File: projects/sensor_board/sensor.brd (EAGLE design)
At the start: 90.2 x 95.9 mm, 49 parts, among them J1 504050-0791, J2 FH28-10S-0.5SH_05_, J3 504050-0791, J4 504050-1091, J5 504050-0791, J6 504050-0791, U1 NXP_FXAS21002CQR1NXP_FXAS2100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, U2 HONEYWELL_HMC5983-TRHONEYWELL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, U3 DS1307N, U4 NXP_FXAS21002CQR1NXP_FXAS2100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, U5 HONEYWELL_HMC5983-TRHONEYWELL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, U6 NXP_FXAS21002CQR1NXP_FXAS2100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, U7 HONEYWELL_HMC5983-TRHONEYWELL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, Y1 ECS-.327-12.5-13X

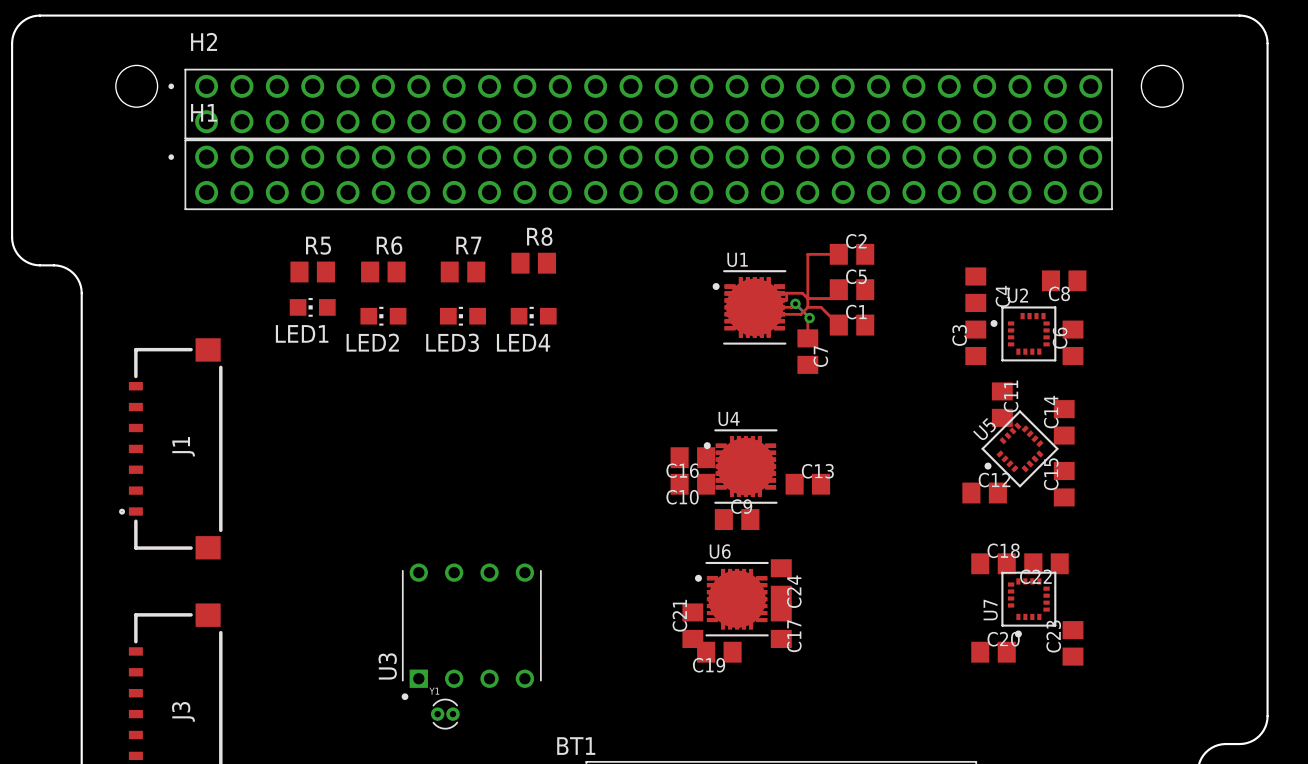
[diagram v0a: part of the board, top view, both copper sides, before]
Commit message: Updates to sensor board. Routed sensors
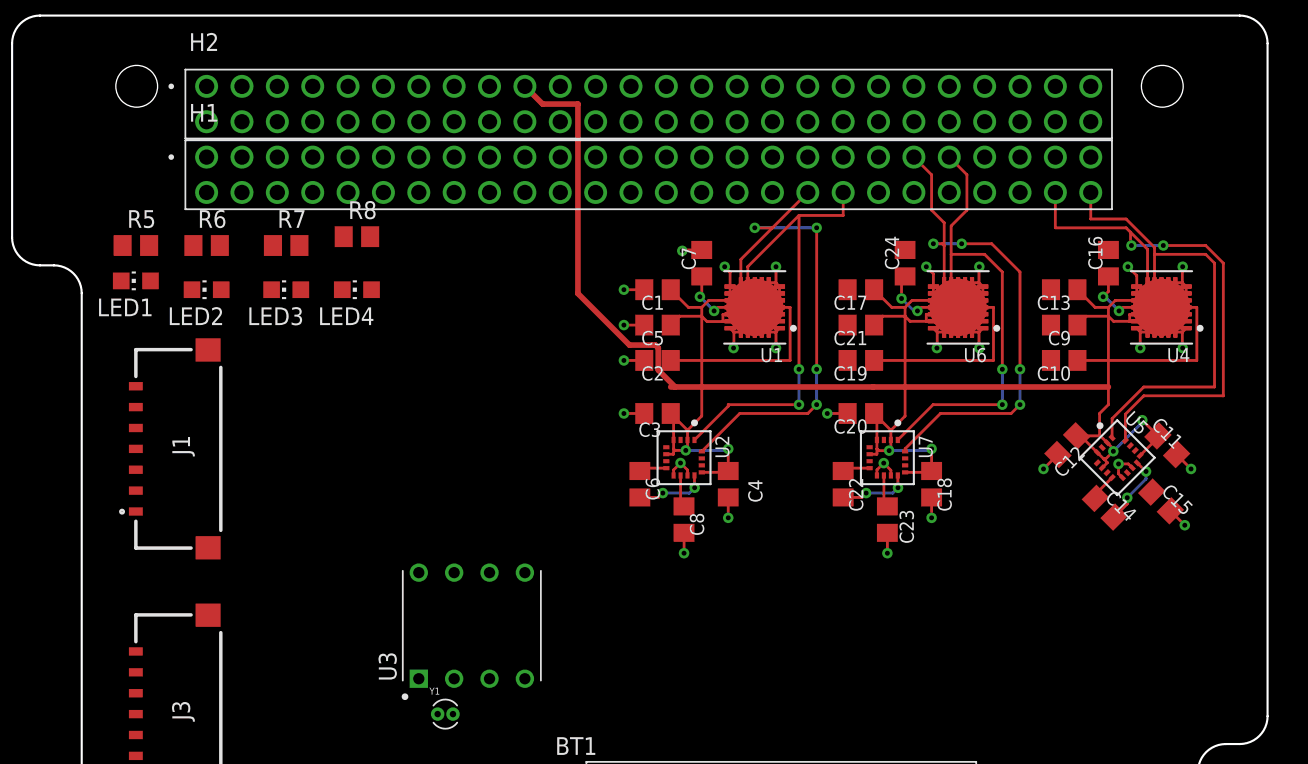
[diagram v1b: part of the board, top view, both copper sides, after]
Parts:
- moved C16 33.0 mm to (78.7, 78.1), turned to 90 degrees
- moved C6 32.7 mm to (45.1, 62.2), turned to 270 degrees
- moved C8 32.2 mm to (48.3, 59.7), turned to 270 degrees
- moved U4 32.0 mm to (82.5, 74.9), turned to 180 degrees
- moved C10 28.1 mm to (75.6, 71.1)
- moved C9 27.3 mm to (75.6, 73.7), turned to 180 degrees
- moved U2 26.3 mm to (48.3, 64.1), turned to 270 degrees
- moved U6 26.3 mm to (67.9, 74.9), turned to 180 degrees
- moved C17 24.8 mm to (61.0, 76.2), turned to 180 degrees
- moved C21 24.7 mm to (61.0, 73.7), turned to 180 degrees
- moved C24 24.5 mm to (64.1, 78.1), turned to 90 degrees
- moved C3 23.4 mm to (46.4, 67.3), turned to 180 degrees
- moved C19 23.3 mm to (61.0, 71.1)
- moved C13 23.1 mm to (75.6, 76.2), turned to 180 degrees
- moved C4 22.6 mm to (51.4, 62.2)
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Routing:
- net 3V3_PDM9: track 16.7 -> 203.7 mm, vias 0 -> 6
- net GND: track 0.00 -> 62.8 mm, vias 0 -> 28
- net I2C3_SDA: track 0.00 -> 39.3 mm, vias 0 -> 2
- net I2C1_SDA: track 0.00 -> 37.1 mm, vias 0 -> 4
- net I2C2_SDA: track 0.00 -> 36.5 mm, vias 0 -> 4
- net I2C2_SCL: track 0.00 -> 33.4 mm, vias 0 -> 2
- net I2C3_SCL: track 0.00 -> 33.0 mm
- net I2C1_SCL: track 0.00 -> 32.3 mm, vias 0 -> 2
- net N$49: track 0.00 -> 5.11 mm, vias 0 -> 2
- net N$45: track 0.00 -> 5.11 mm, vias 0 -> 2
- net N$47: track 0.00 -> 5.11 mm, vias 0 -> 2
- net N$67: track 0.00 -> 4.56 mm, vias 0 -> 2
- net N$72: track 0.00 -> 4.46 mm, vias 0 -> 2
- net N$56: track 0.00 -> 2.32 mm
- net N$52: track 0.00 -> 2.32 mm
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
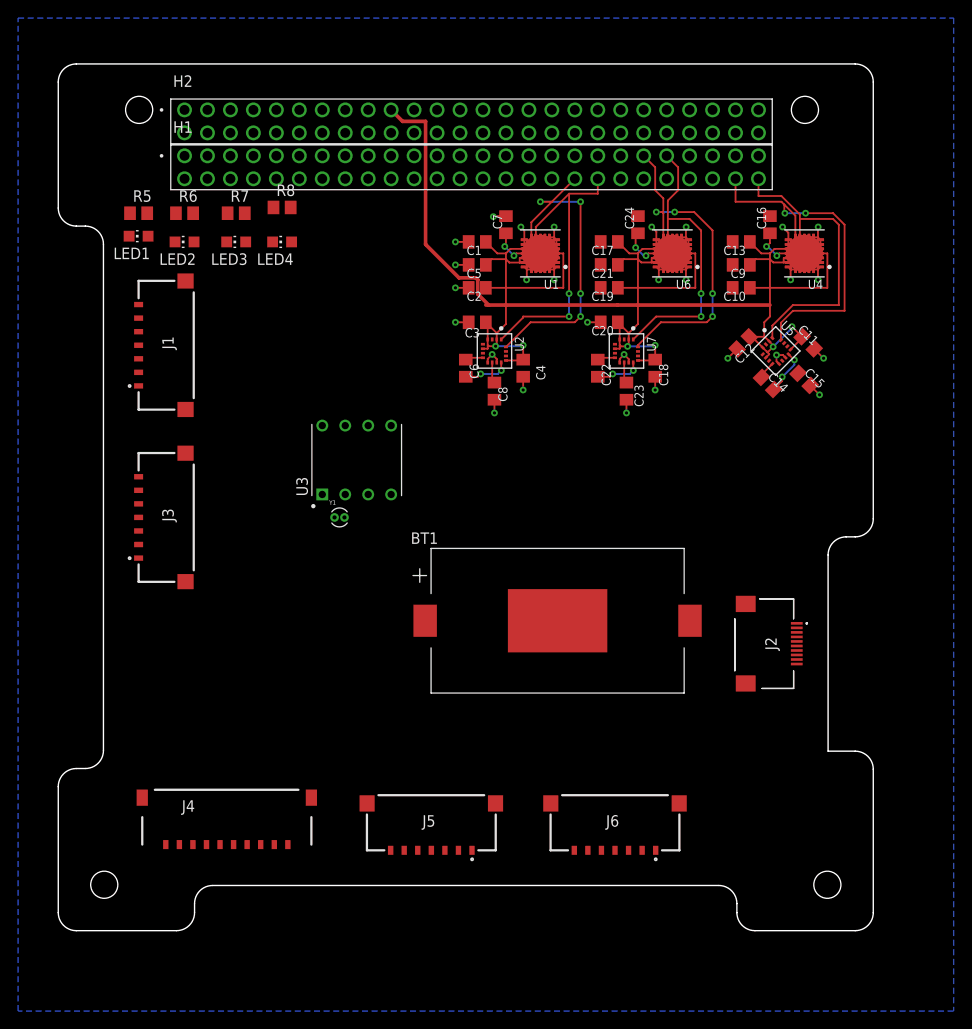
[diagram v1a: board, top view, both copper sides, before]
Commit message: Updated sensor board. First revision of completely routed board
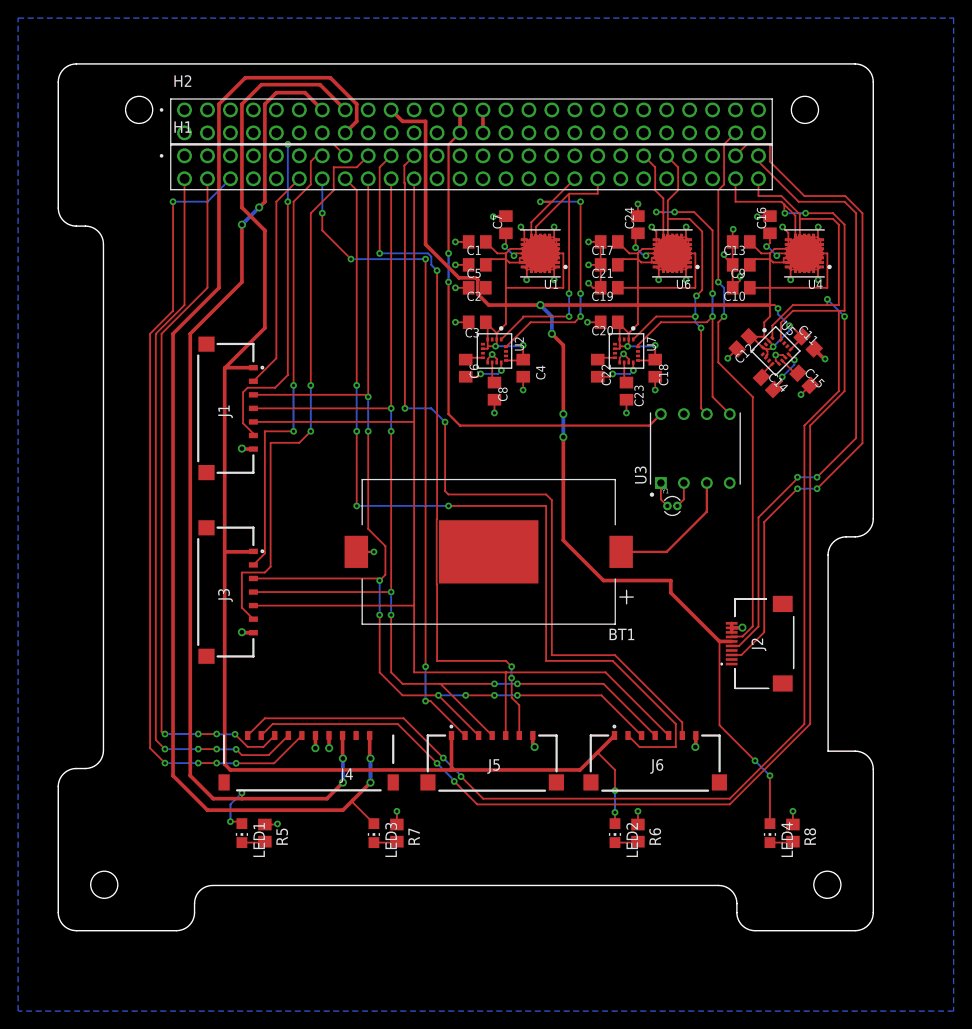
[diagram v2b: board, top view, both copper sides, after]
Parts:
- moved R8 89.4 mm to (81.3, 10.8), turned to 270 degrees
- moved R6 85.0 mm to (64.1, 10.8), turned to 270 degrees
- moved LED4 84.8 mm to (78.7, 10.8), turned to 180 degrees
- moved LED2 80.9 mm to (61.6, 10.8), turned to 180 degrees
- moved R7 70.8 mm to (37.5, 10.8), turned to 270 degrees
- moved R5 70.0 mm to (22.9, 10.8), turned to 270 degrees
- moved LED3 67.2 mm to (34.9, 10.8), turned to 180 degrees
- moved LED1 67.0 mm to (20.3, 10.8), turned to 180 degrees
- moved U3 37.5 mm to (70.5, 53.3)
- moved Y1 36.9 mm to (67.9, 47.0)
- moved J3 15.1 mm to (21.6, 37.5), turned to 90 degrees
- moved J1 14.5 mm to (21.6, 57.8), turned to 90 degrees
- moved J5 14.4 mm to (48.0, 21.6), turned to 180 degrees
- moved J6 13.5 mm to (66.0, 21.6), turned to 180 degrees
- moved J4 12.9 mm to (21.0, 21.6), turned to 180 degrees
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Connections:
- net CHASSIS: now also H2.50; no longer H1.29, H1.30
- net DTR: now also H1.6; no longer H1.23
- net UART3_RX: now also H1.51; no longer H1.8
- net UART3_TX: now also H1.49; no longer H1.6
- net UART8_RX: now also H1.4; no longer H1.11
- net UART8_TX: now also H1.2; no longer H1.9
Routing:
- net 5V_PDM6: track 0.00 -> 153.2 mm, vias 0 -> 2
- net 5V_PDM7: track 0.00 -> 131.2 mm, vias 0 -> 2
- net SPI_SCK: track 0.00 -> 128.2 mm
- net SPI_MISO: track 0.00 -> 125.3 mm, vias 0 -> 6
- net SPI_MOSI: track 0.00 -> 120.7 mm, vias 0 -> 8
- net I2C3_SCL: track 33.0 -> 151.7 mm, vias 0 -> 4
- net I2C3_SDA: track 39.3 -> 156.2 mm, vias 2 -> 4
- net 5V_PDM5: track 0.00 -> 115.0 mm, vias 0 -> 6
- net SPI_EN_4: track 0.00 -> 100.4 mm, vias 0 -> 4
- net SPI_SS_4: track 0.00 -> 89.4 mm, vias 0 -> 2
- net DTR: track 0.00 -> 87.7 mm, vias 0 -> 5
- net UART8_TX: track 0.00 -> 79.7 mm, vias 0 -> 4
- net SPI_SS_3: track 0.00 -> 78.7 mm, vias 0 -> 4
- net UART8_RX: track 0.00 -> 77.0 mm, vias 0 -> 4
- net UART3_TX: track 0.00 -> 75.6 mm, vias 0 -> 2
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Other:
- board text added: "IMG"
- board text added: "MTQ"
- board text added: "RWA"
- board text added: "SENS"

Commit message: Added oshpark 2 layer design rule, updated gyroscope library, added new gyroscope footprint to sensor board
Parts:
- U1, U4, U6: value NXP_FXAS21002CQR1NXP_FXAS21002CQR1_0_0 -> NXP_FXAS21002CQR1_EDITEDNXP_FXAS21002CQR1_0_0; device NXP - FXAS21002CQR1:NXP_FXAS21002CQR1_0 -> NXP - FXAS21002CQR1:NXP_FXAS21002CQR1_0_EDITED
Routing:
- net GND: track 103.0 -> 100.2 mm
- net 3V3_PDM9: track 277.4 -> 279.3 mm
- net I2C3_SCL: track 151.7 -> 151.2 mm

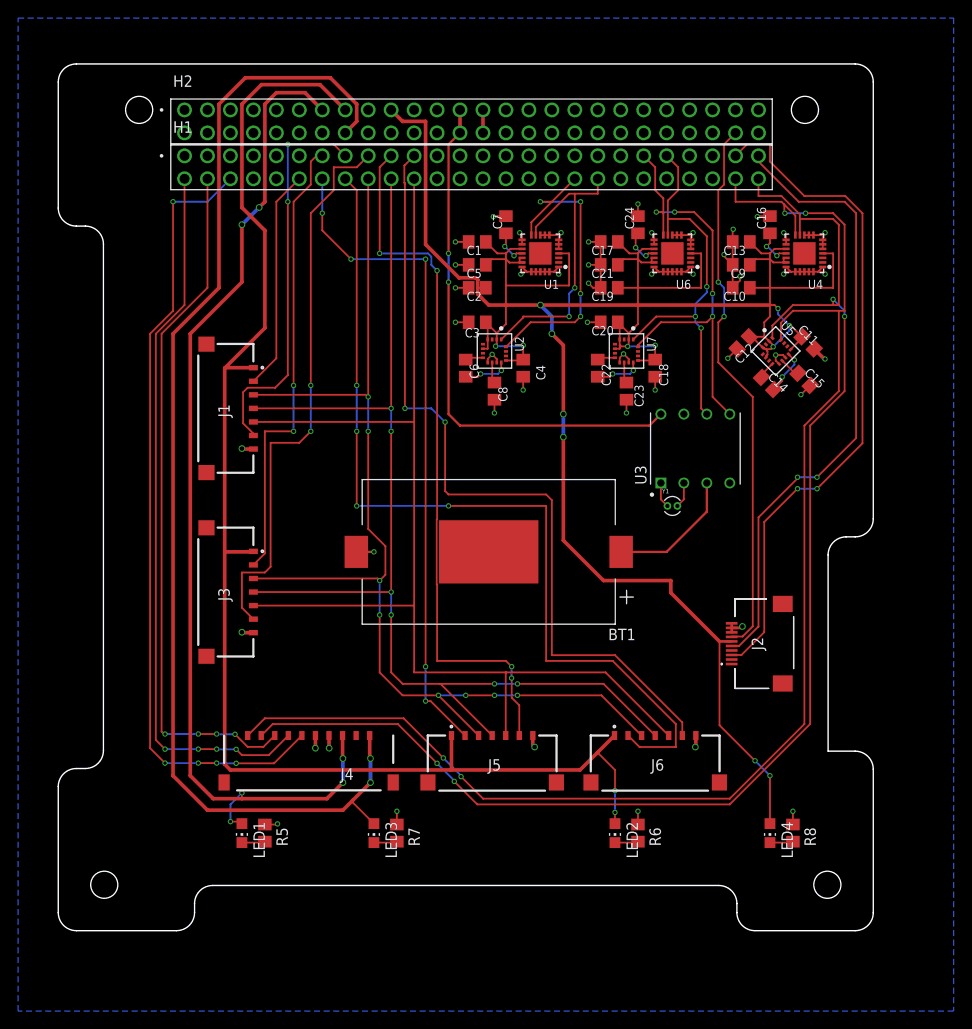
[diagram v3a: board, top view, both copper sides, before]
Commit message: Converted sensor board to 4 layers. Re-routed magnetometers/gyros and ripped up most other traces
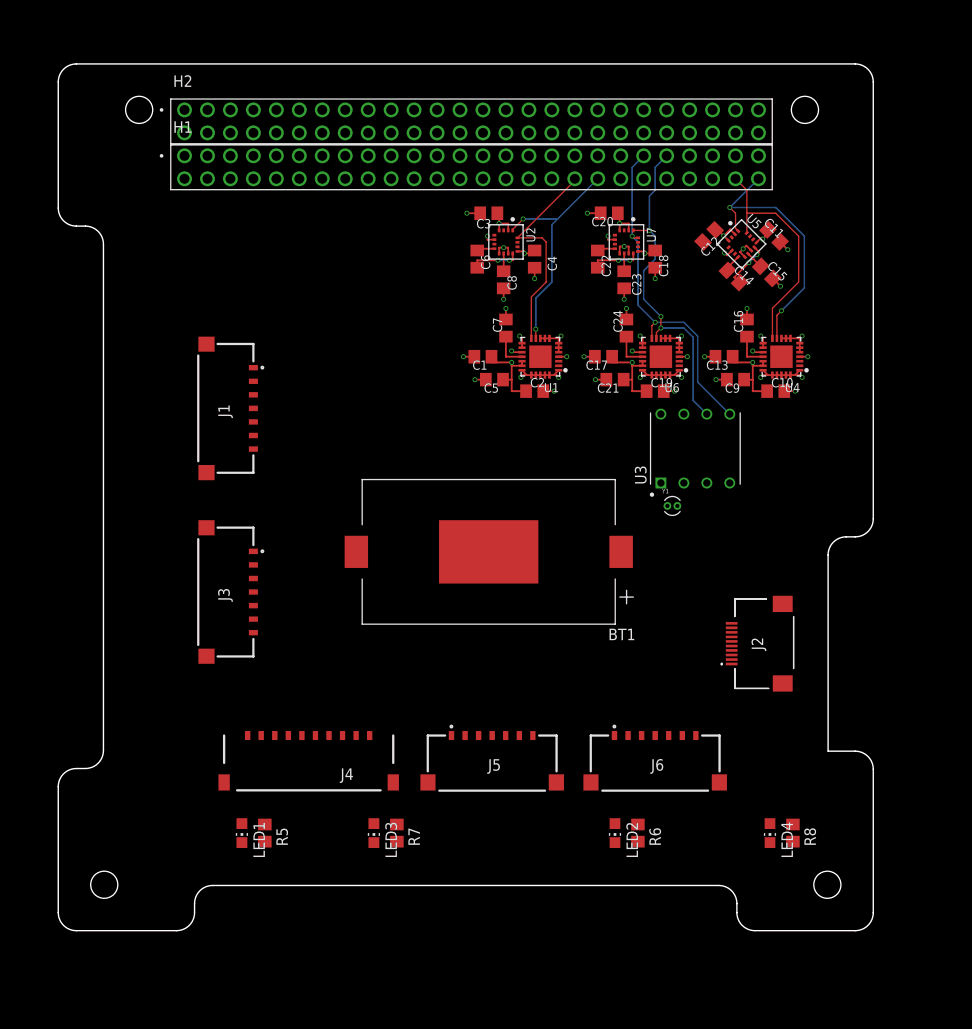
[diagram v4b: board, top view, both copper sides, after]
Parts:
- moved C2 13.1 mm to (52.7, 59.7), turned to 0 degrees
- moved C13 12.8 mm to (73.7, 63.5)
- moved C5 12.8 mm to (48.3, 61.0)
- moved C1 12.7 mm to (47.0, 63.5)
- moved C17 12.7 mm to (60.3, 63.5)
- moved C21 12.7 mm to (61.6, 61.0)
- moved C9 12.7 mm to (74.9, 61.0)
- moved C15 12.5 mm to (78.4, 72.8)
- moved C19 12.5 mm to (66.0, 59.7), turned to 0 degrees
- moved C12 12.4 mm to (72.0, 76.9)
- moved U5 12.4 mm to (75.6, 76.0)
- moved C11 12.4 mm to (79.2, 76.9)
- moved C14 12.4 mm to (74.7, 72.4)
- moved C8 12.4 mm to (49.3, 72.0)
- moved C23 12.3 mm to (62.6, 72.0)
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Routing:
- net 3V3_PDM9: track 279.3 -> 60.8 mm, vias 13 -> 18
- net 5V_PDM6: track 153.2 -> 0.00 mm, vias 2 -> 0
- net 5V_PDM7: track 131.2 -> 0.00 mm, vias 2 -> 0
- net I2C3_SDA: track 155.9 -> 25.8 mm, vias 4 -> 0
- net SPI_SCK: track 128.2 -> 0.00 mm
- net SPI_MISO: track 125.3 -> 0.00 mm, vias 6 -> 0
- net I2C3_SCL: track 151.2 -> 29.6 mm, vias 4 -> 2
- net SPI_MOSI: track 120.7 -> 0.00 mm, vias 8 -> 0
- net 5V_PDM5: track 115.0 -> 0.00 mm, vias 6 -> 0
- net SPI_EN_4: track 100.4 -> 0.00 mm, vias 4 -> 0
- net SPI_SS_4: track 89.4 -> 0.00 mm, vias 2 -> 0
- net DTR: track 87.7 -> 0.00 mm, vias 5 -> 0
- net UART8_TX: track 79.7 -> 0.00 mm, vias 4 -> 0
- net SPI_SS_3: track 78.7 -> 0.00 mm, vias 4 -> 0
- net UART8_RX: track 77.0 -> 0.00 mm, vias 4 -> 0
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- added copper zone on layer 15, net 3V3_PDM9
- added copper zone on layer 2, net GND
- removed copper zone on layer 16, net GND

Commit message: Completed first revision of 4 layer sensor board
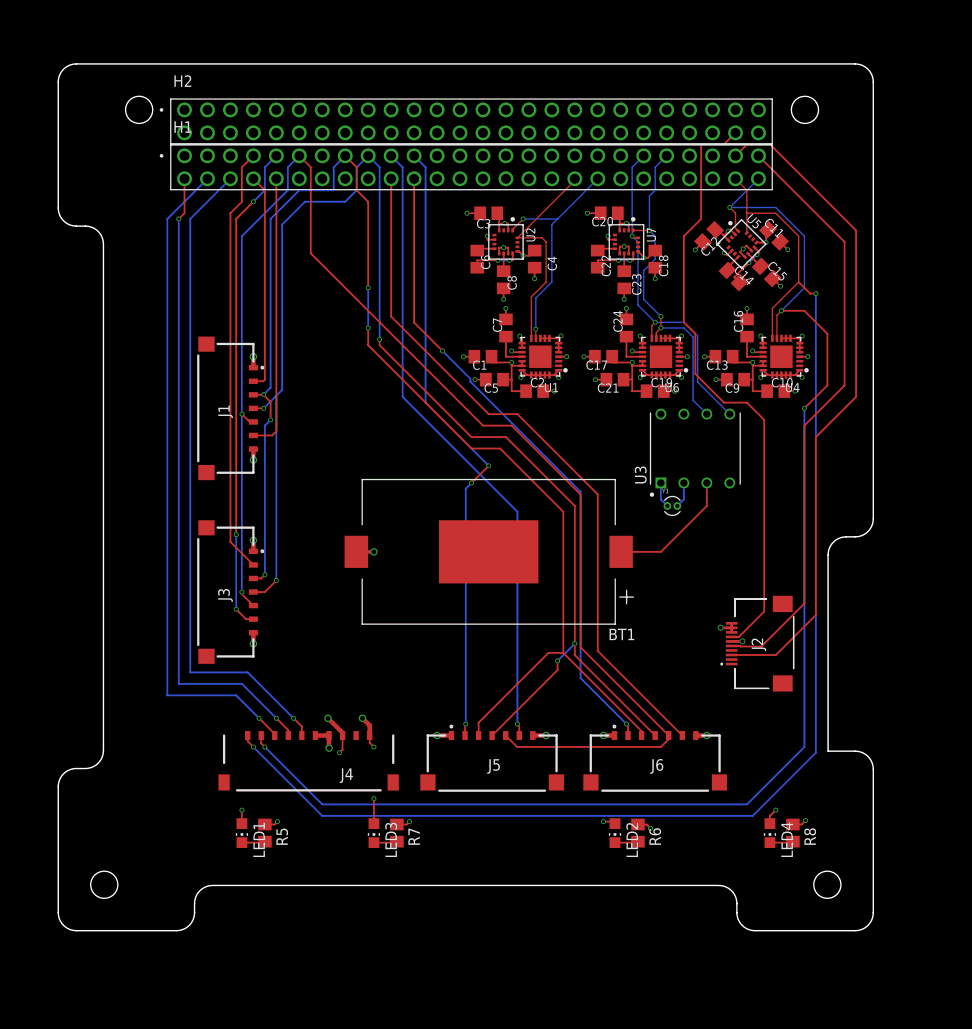
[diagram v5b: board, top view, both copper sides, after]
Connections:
- net SPI_EN_1: now also H1.8; no longer H1.12
- net SPI_EN_2: now also H1.7; no longer H1.13
- net SPI_EN_3: now also H1.21; no longer H1.14
- net SPI_EN_4: now also H1.22; no longer H1.16
- net SPI_MISO: now also H1.17; no longer H1.20
- net SPI_MOSI: now also H1.15; no longer H1.18
- net SPI_SCK: now also H1.11; no longer H1.22
- net SPI_SS_1: now also H1.10; no longer H1.15
- net SPI_SS_2: now also H1.9; no longer H1.17
- net SPI_SS_4: now also H1.20; no longer H1.21
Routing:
- net SPI_SCK: track 0.00 -> 156.8 mm, vias 0 -> 2
- net SPI_MISO: track 0.00 -> 153.4 mm, vias 0 -> 5
- net SPI_MOSI: track 0.00 -> 149.0 mm, vias 0 -> 5
- net I2C3_SDA: track 25.8 -> 148.9 mm, vias 0 -> 2
- net I2C3_SCL: track 29.6 -> 148.9 mm, vias 2 -> 4
- net SPI_SS_4: track 0.00 -> 76.8 mm
- net UART8_RX: track 0.00 -> 72.8 mm, vias 0 -> 1
- net DTR: track 0.00 -> 72.3 mm, vias 0 -> 1
- net SPI_EN_4: track 0.00 -> 71.4 mm, vias 0 -> 2
- net UART8_TX: track 0.00 -> 71.0 mm, vias 0 -> 2
- net UART3_TX: track 2.54 -> 73.3 mm
- net SPI_SS_3: track 0.00 -> 70.0 mm, vias 0 -> 1
- net SPI_EN_3: track 0.00 -> 68.6 mm, vias 0 -> 3
- net CHASSIS: track 0.00 -> 66.7 mm
- net UART3_RX: track 0.00 -> 65.4 mm
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- added copper zone on layer 15, net 5V_PDM5
- added copper zone on layer 15, net 5V_PDM6
- added copper zone on layer 15, net 5V_PDM7
